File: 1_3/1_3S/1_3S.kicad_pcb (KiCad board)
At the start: 2 copper layers, 137.5 x 91.4 mm, 52 parts, among them SW1 SW_SPST, SW10 SW_SPST, SW11 SW_SPST, SW12 SW_SPST, SW13 SW_SPST, SW14 SW_SPST, SW15 SW_SPST, SW16 SW_SPST, SW17 SW_SPST, SW18 SW_SPST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

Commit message: 1_3S rebuild
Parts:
- removed D1, D13, D7: D_Small, Two:Diode_TH_SMD_DUAL
- removed SW1, SW13, SW7: SW_SPST, Two:KS-27_KS-33_Hotswap_1U_DUAL
- moved H2 18.4 mm to (112.4, 95.5)
- moved H1 18.3 mm to (112.3, 76.5)
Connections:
- U1 pad 1: C0 -> unconnected-(U1-A2/0.02_H-Pad1)
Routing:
- net C0: track 220.5 -> 0.00 mm, vias 5 -> 0
- net R2: track 190.7 -> 166.3 mm, vias 7 -> 6
- net R0: track 193.6 -> 169.9 mm, vias 8 -> 7
- net R1: track 183.0 -> 160.7 mm, vias 7 -> 6
- net Net-(D13-A): track 19.3 -> 0.00 mm, vias 2 -> 0
- net Net-(D1-A): track 15.9 -> 0.00 mm, vias 2 -> 0
- net Net-(D7-A): track 15.7 -> 0.00 mm, vias 2 -> 0
- net C1: track 199.9 -> 208.1 mm, vias 6 -> 4
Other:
- board size 137.5 x 91.4 mm -> 118.5 x 91.4 mm
- board text added: "Ergonaut One S v1.3 by yumagulovrn"
- board text removed: "Ergonaut One v1.3 by yumagulovrn"

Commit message: S chk
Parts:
- moved H4 0.46 mm to (186.2, 116.0)
- moved H3 0.25 mm to (170.5, 74.3)
- moved D2 0.20 mm to (103.5, 77.3)
- moved D8 0.13 mm to (103.5, 81.2)
- moved H1 0.08 mm to (112.4, 76.5)
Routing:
- net R1: track 160.7 -> 161.3 mm

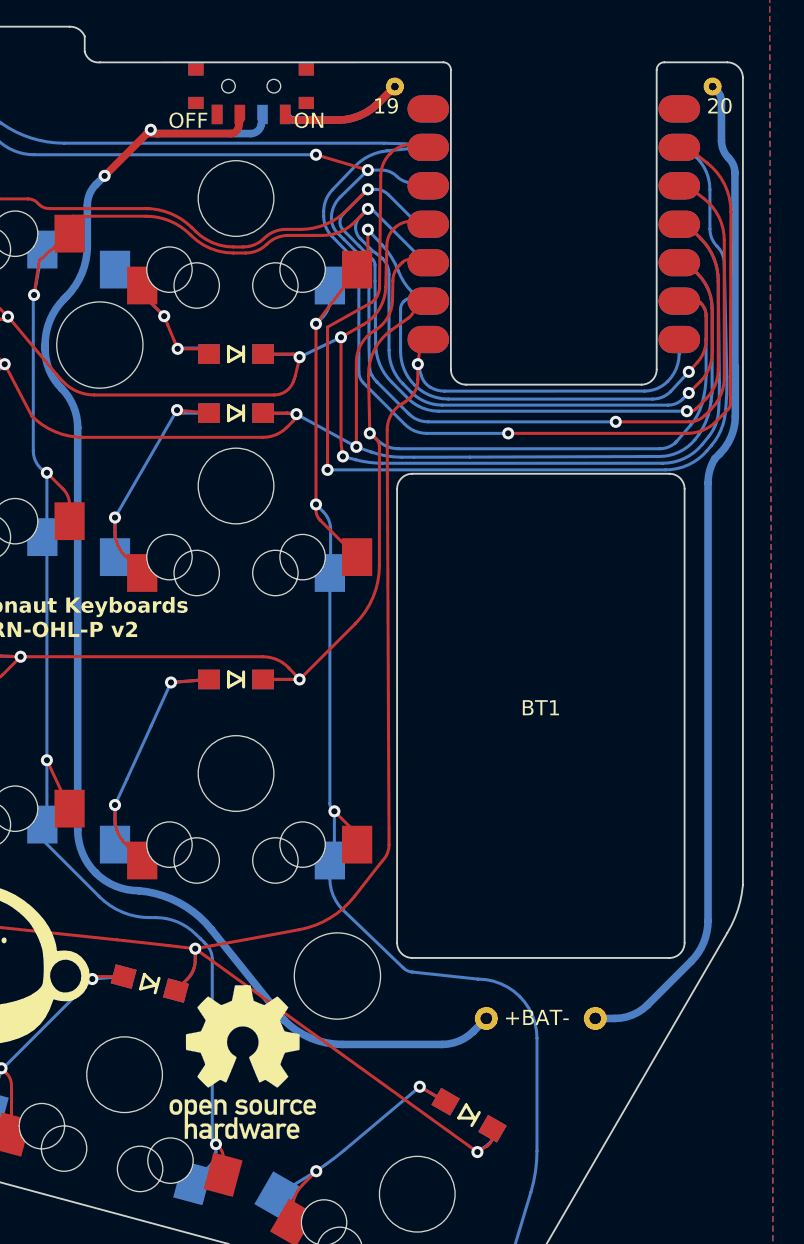
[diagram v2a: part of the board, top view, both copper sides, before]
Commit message: adjust d19,20,21 all
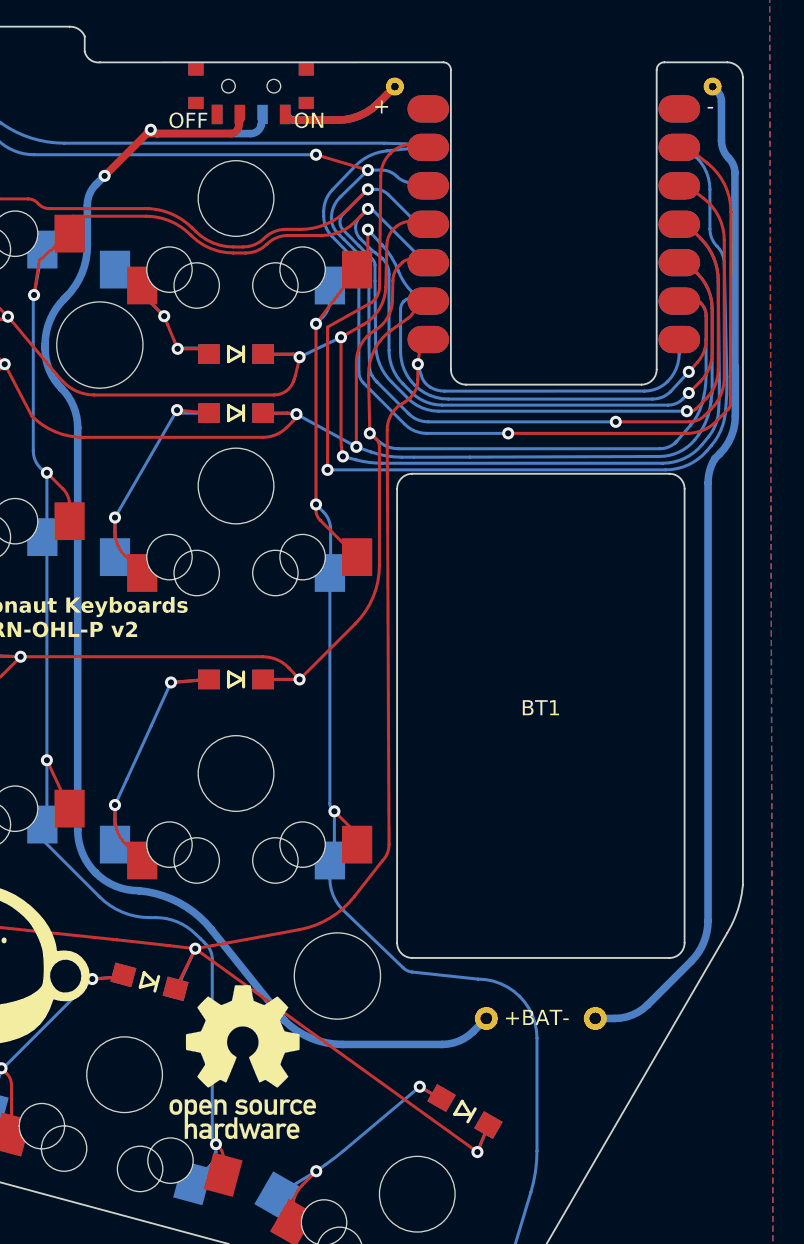
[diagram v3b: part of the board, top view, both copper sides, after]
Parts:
- moved D21 0.36 mm to (194.6, 125.0)
- moved D20 0.11 mm to (173.8, 116.4)
